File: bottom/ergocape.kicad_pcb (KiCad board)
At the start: 2 copper layers, 183.2 x 140.8 mm, 10 parts

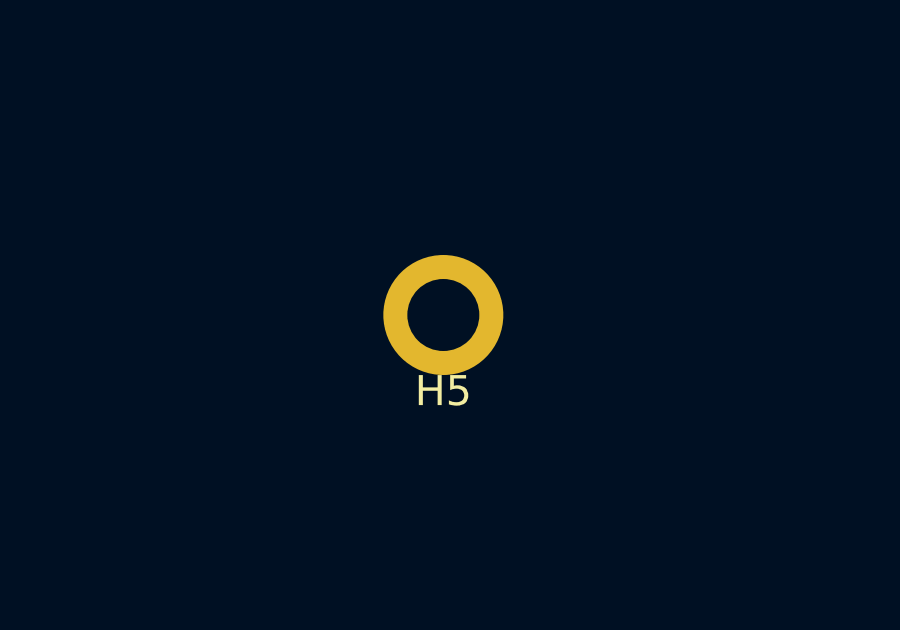
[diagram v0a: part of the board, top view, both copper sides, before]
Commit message: Change in layout and design, remove atmega32u4
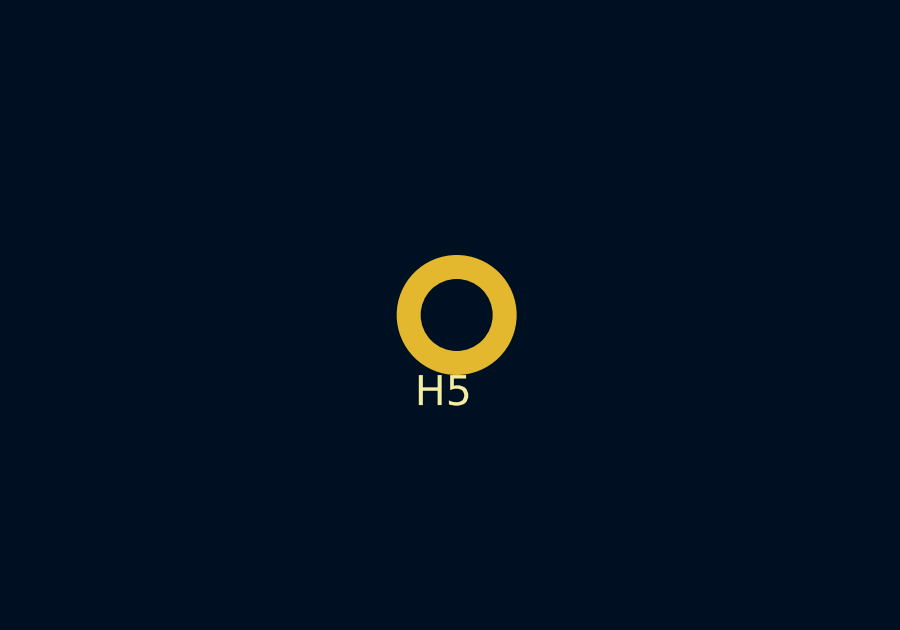
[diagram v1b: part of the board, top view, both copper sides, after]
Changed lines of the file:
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@@
     (mod_text_size 1 1)
     (mod_text_width 0.15)
-    (pad_size 5.2 5.2)
-    (pad_drill 4.7)
+    (pad_size 4 4)
+    (pad_drill 2.4)
     (pad_to_mask_clearance 0.051)
     (solder_mask_min_width 0.25)
@@
       (effects (font (size 1 1) (thickness 0.15)))
     )
-    (pad "" thru_hole circle (at 0 0) (size 4 4) (drill 2.4) (layers *.Cu *.Mask))
+    (pad "" thru_hole circle (at 0.4445 0) (size 4 4) (drill 2.4) (layers *.Cu *.Mask))
   )
   (module usbc_footprint:mount_hole_2.4x4 (layer F.Cu)

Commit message: cleanup and finish the case files
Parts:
- H1, H10, H11, H12, H2, H3, H5, H6, H8, H9: footprint usbc_footprint:mount_hole_2.4x4 -> acheron_MountingHoles:MountingHole_2.5x4.0mm
- moved H10 16.1 mm to (39.6, 60.5)
- moved H11 14.2 mm to (39.9, 20.2)
- moved H5 0.70 mm to (113.9, 60.7)
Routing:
- added copper zone on B.Cu, net (none)
- added copper zone on F.Cu, net (none)
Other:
- outline, holes or cut-outs redrawn

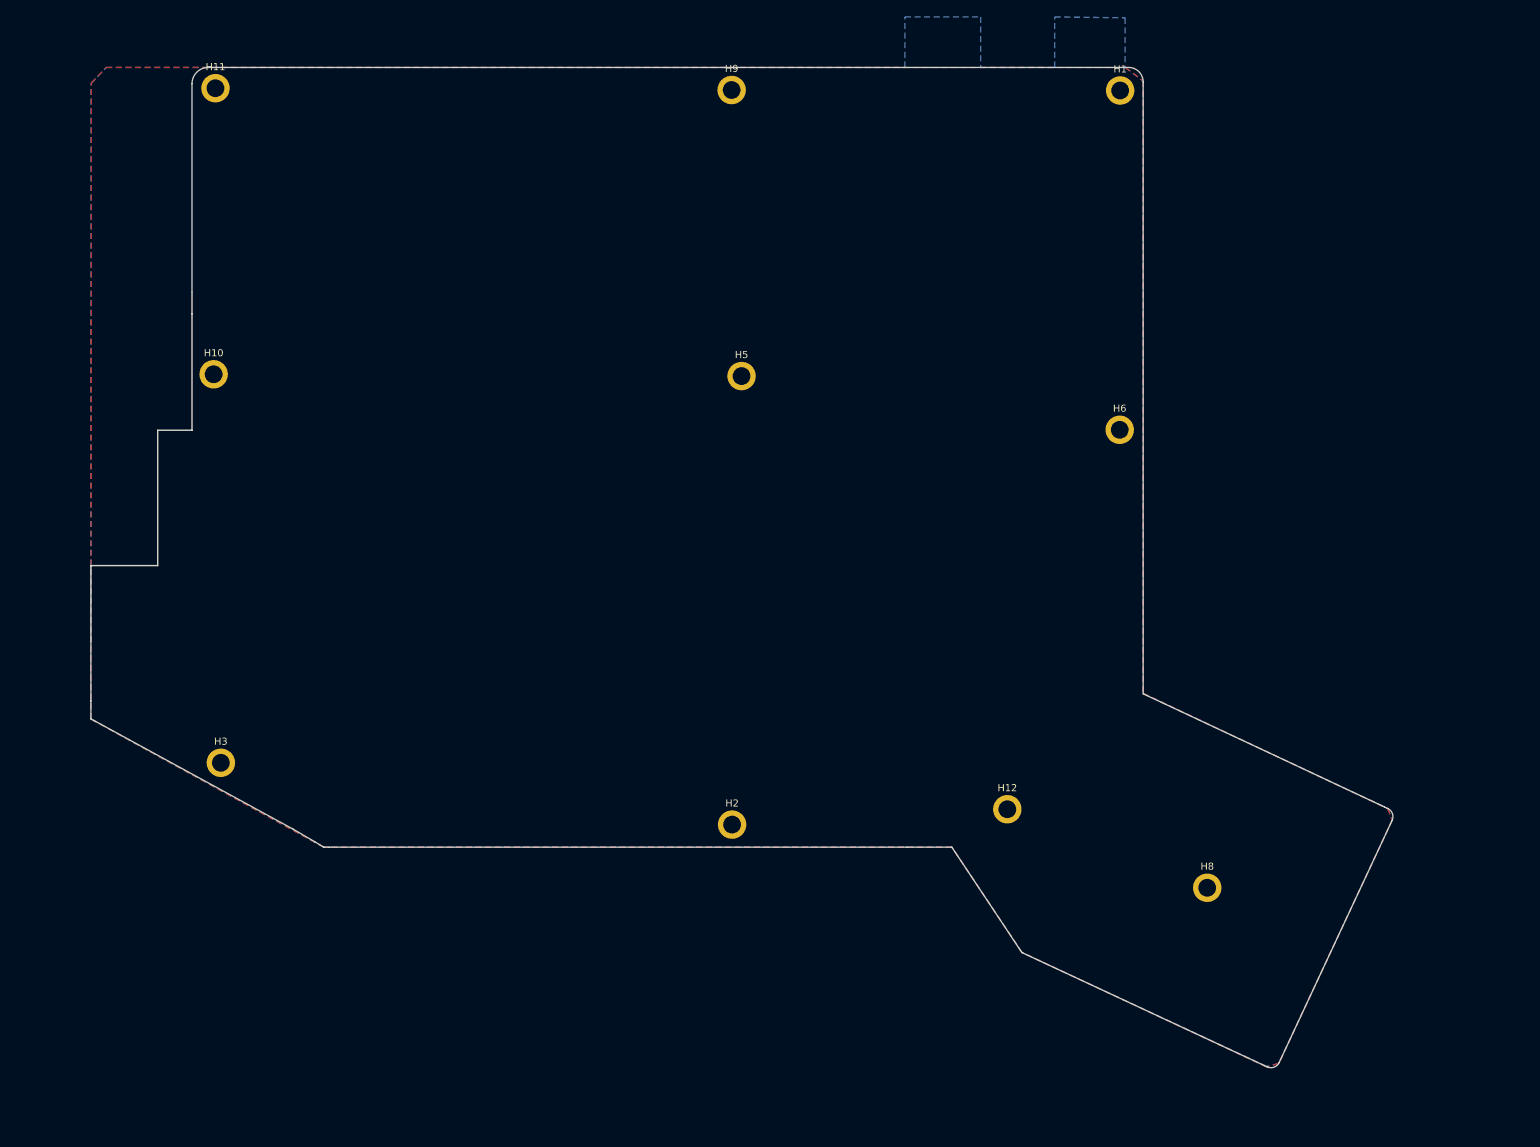
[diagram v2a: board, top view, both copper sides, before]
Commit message: finalize plate and mounting holes
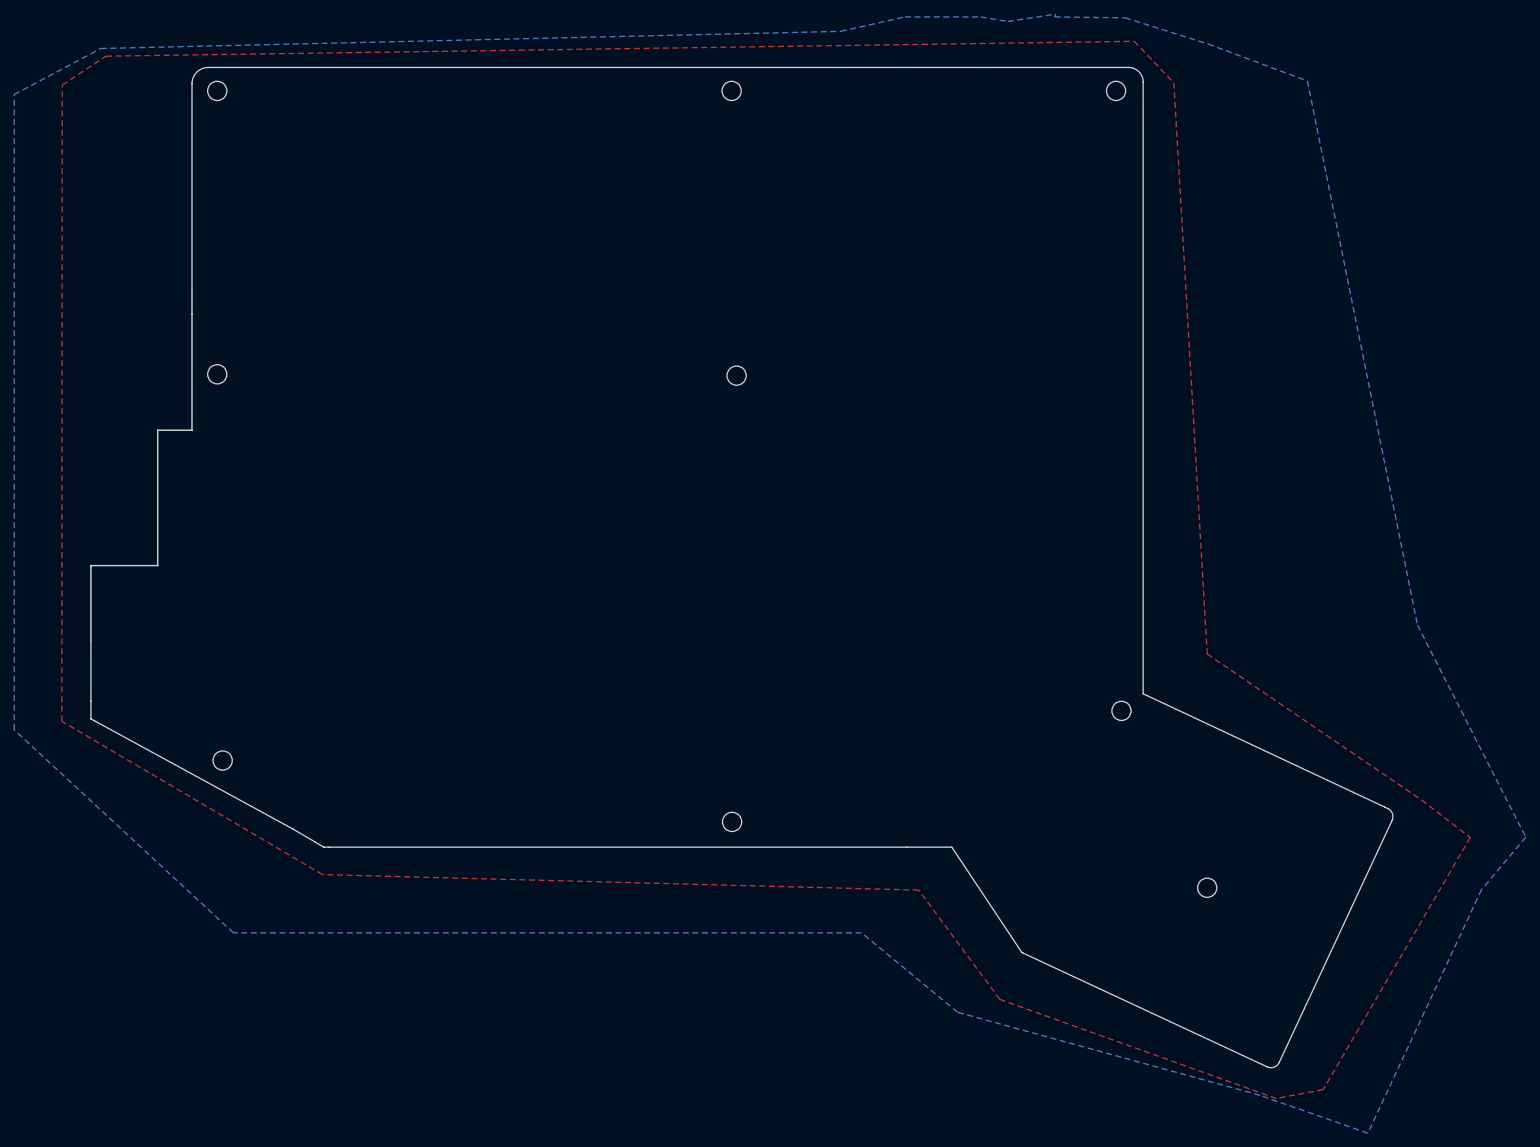
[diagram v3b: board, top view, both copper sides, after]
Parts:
- removed H6: MountingHole, acheron_MountingHoles:MountingHole_2.5x4.0mm
- H1, H10, H11, H12, H2, H3, H5, H8, H9: footprint acheron_MountingHoles:MountingHole_2.5x4.0mm -> MountingHole:MountingHole_2.7mm_M2.5
- moved H12 21.2 mm to (167.4, 107.8)
- moved H5 0.70 mm to (113.2, 60.6)
- moved H1 0.58 mm to (166.6, 20.6)
- moved H10 0.51 mm to (40.1, 60.5)
- moved H11 0.46 mm to (40.1, 20.6)
- moved H3 0.41 mm to (40.9, 114.8)
- moved H2 0.38 mm to (112.6, 123.4)
- moved H9 0.13 mm to (112.5, 20.6)
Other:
- outline, holes or cut-outs redrawn
